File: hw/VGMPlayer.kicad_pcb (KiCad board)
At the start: 4 copper layers, 40 x 67 mm, 91 parts, among them J1 Micro_SD_Card, J2 EarPiece, P1 USB_C_Receptacle_16P, P2 SWD, P3 BATT, P4 UART, P5 ICSP, P6 CODEC, Q1 2N7002, Q2 AO3401A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

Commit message: 2nd version, change KBC functions
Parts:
- removed P4: UART, BZ_Connector:PINHDR-THT-50mil-01x02
- removed the R20 at (149.6, 100.6)
- added M1: Mechanical-NC, BZ_Mechanical:Hole-Mech_0.5, B.Cu at (131.5, 100.4)
- added R25: 1K, BZ_Resistor:R_0402, B.Cu at (131.8, 90.0)
- added R26: 1K, BZ_Resistor:R_0402, B.Cu at (131.8, 91.5)
- added S5: RESET, BZ_Switch:C&K_PTS525, F.Cu at (150.0, 127.5)
- C24, C34: value 10n -> DNP
- C25, C35: value 4.7u -> 10u
- C3, C4: value 33p -> 22p
- P2: footprint BZ_Connector:PINHDR-THT-50mil-01x05 -> BZ_Connector:PINHDR-THT-50mil-02x05
- R10, R9: value 2K -> 2K2
- R20: renamed from R21; value 2K -> 2K2
- TP1: footprint BZ_Misc:TE_RCT0805 -> BZ_Misc:TP_THT-Pad-0.8
- TP2: value BAT+ -> TP; footprint BZ_Misc:TE_RCT0805 -> BZ_Misc:TP_THT-Pad-0.8
- TP3: value BAT- -> TP; footprint BZ_Misc:TE_RCT0805 -> BZ_Misc:TP_THT-Pad-0.8
- U3, U7: value TPS79933DDCR -> LP5907MFX-3.3
- U5: value TP4057 -> MCP73831-OT; footprint BZ_Standard_IC:SOT-23-6 -> BZ_Standard_IC:SOT-23-5
- moved TP3 3.72 mm to (168.7, 96.7), turned to 270 degrees
- moved S3 3.00 mm to (142.0, 127.5), turned to 90 degrees
- moved S4 3.00 mm to (158.0, 127.5), turned to 270 degrees
- moved S2 2.30 mm to (150.0, 133.2)
- moved S1 2.30 mm to (150.0, 121.8)
- moved Y1 1.10 mm to (142.3, 104.3)
- moved C11 1.10 mm to (138.9, 103.3)
- moved C12 1.10 mm to (145.2, 98.7)
- moved C13 1.10 mm to (145.2, 94.9)
- moved C3 1.10 mm to (144.5, 103.3)
- moved C4 1.10 mm to (144.5, 105.3)
- moved C6 1.10 mm to (137.7, 103.3)
- moved R10 1.10 mm to (137.7, 105.3)
- moved R6 1.10 mm to (136.5, 103.3)
- moved R7 1.10 mm to (140.1, 103.3)
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- renumbered R22 to R21, R23 to R22, R24 to R23, R25 to R24
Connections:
- P2 pad 2: /SWCLK -> /SWDIO
- P2 pad 4: /SWDIO -> /SWCLK
- P2 pad 5: /RUN -> Net-(P2-Pad5)
- Q2 pad 2: VIN -> VBAT
- Q2 pad 3: VBAT -> VIN
- R20 pad 2: Net-(R21-Pad2) -> Net-(R20-Pad2)
- R21 pad 1: Net-(R21-Pad2) -> Net-(R20-Pad2)
- S4 pad 2: Net-(R20-Pad2) -> Net-(S4-Pad2)
- U5 pad 1: /CHG_CHRG -> (no net)
- U5 pad 5: (no net) -> Net-(R20-Pad2)
- U6 pad 2: /CHG_CHRG -> Net-(S4-Pad2)
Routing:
- net Net-(S4-Pad2): track 0.00 -> 37.7 mm, vias 0 -> 1
- net Net-(R20-Pad2): track 39.1 -> 3.88 mm, vias 1 -> 0
- net /VPP: track 30.0 -> 57.3 mm, vias 1 -> 3
- net /CHG_CHRG: track 18.3 -> 0.00 mm, vias 2 -> 0
- net VBAT: track 107.6 -> 95.2 mm, vias 3 -> 4
- net GND: track 182.5 -> 194.4 mm, vias 61 -> 58
- net Net-(P2-Pad8): track 0.00 -> 9.09 mm
- net 3V3: track 134.1 -> 141.5 mm
- net Net-(P2-Pad5): track 0.00 -> 7.23 mm, vias 0 -> 1
- net Net-(D2-PadK): track 51.2 -> 47.0 mm
- net /ICSPDAT: track 51.5 -> 47.4 mm
- net Net-(R21-Pad2): track 3.88 -> 0.00 mm
- net /SWDIO: track 7.32 -> 10.5 mm
- net Net-(S2-Pad2): track 37.7 -> 35.6 mm
- net /SD_DAT0: track 21.0 -> 19.0 mm
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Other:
- board text added: "C"
- board text added: "D"
- board text added: "E"
- board text added: "G"
- board text added: "V"
- board text added: "VGMPlayer 20210604"
- board text removed: "+USB"
- board text removed: "3V"
- board text removed: "3V3"
- board text removed: "BOOTSEL"
- board text removed: "CLK"
- board text removed: "DFU"
- board text removed: "DIO"
- board text removed: "Dev. Mode"
- board text removed: "EN"
- board text removed: "GD"
- board text removed: "GND"
- board text removed: "IO"
- board text removed: "RUN"
- board text removed: "TEST"
- board text removed: "VGMPlayer 20210517"

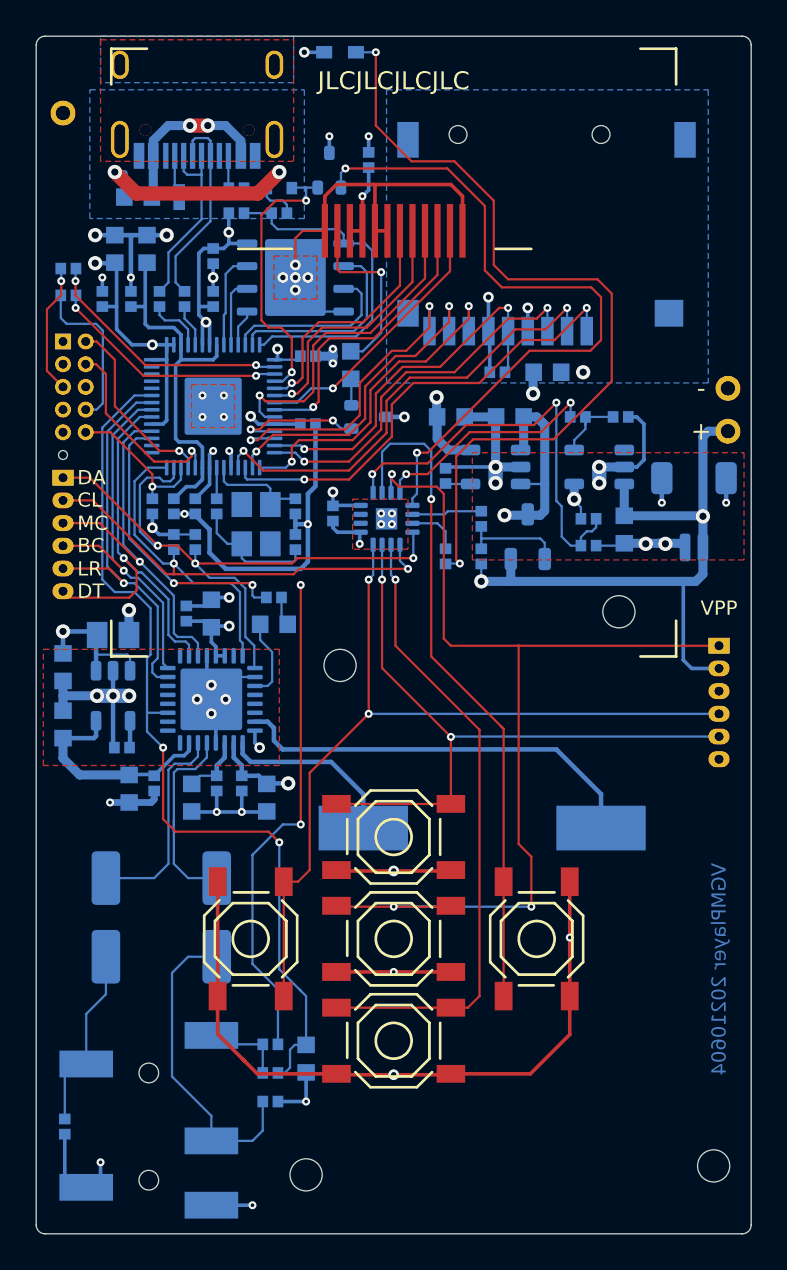
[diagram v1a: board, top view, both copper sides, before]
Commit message: Using Molex Picoblade 1.25 connector
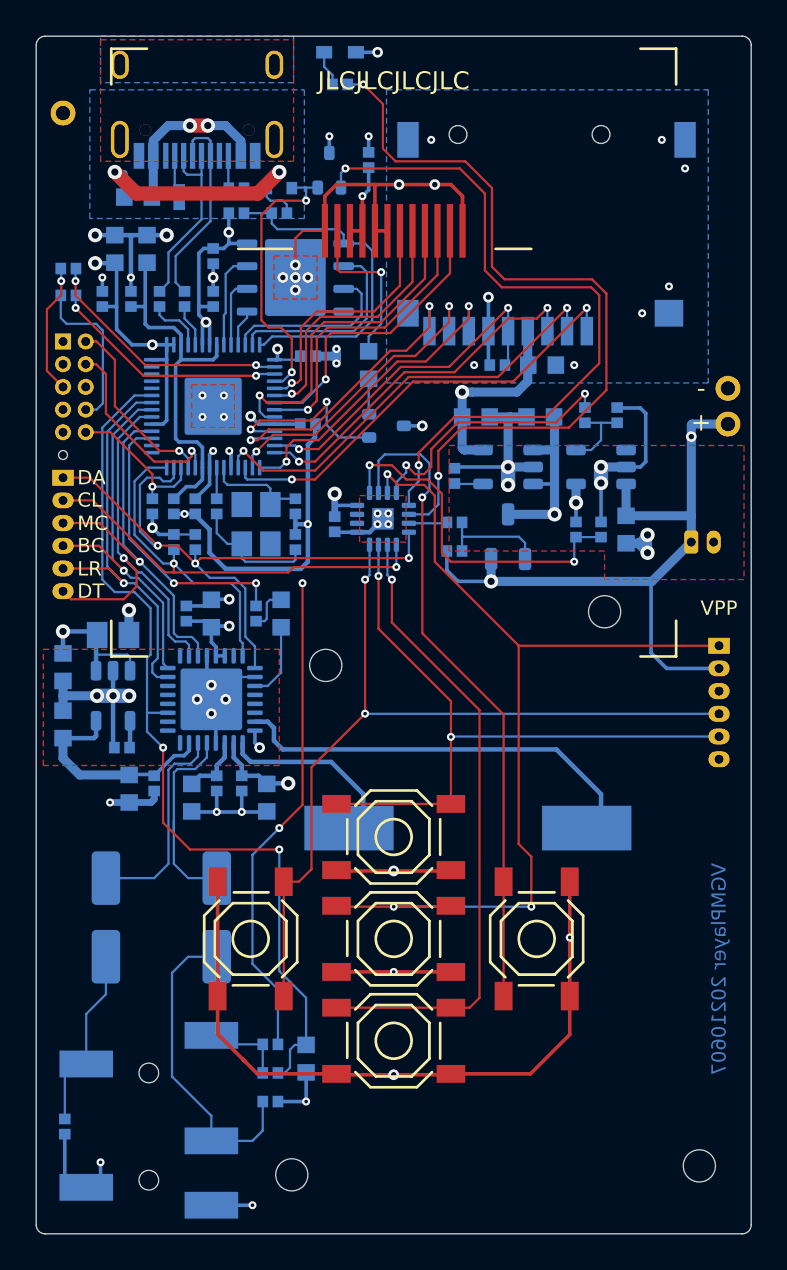
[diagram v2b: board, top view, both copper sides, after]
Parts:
- P3: footprint BZ_Connector:JST_SM02B-SRSS-TB -> BZ_Connector:MLX_PicoBlade-Horz-01x02-1.25P
- moved R24 27.1 mm to (147.0, 79.7), turned to 0 degrees
- moved P3 1.71 mm to (166.7, 105.3)
- moved C33 1.70 mm to (158.2, 98.3)
- moved R22 1.53 mm to (153.4, 105.8), turned to 0 degrees
- moved R23 1.51 mm to (153.4, 104.2), turned to 180 degrees
- moved C35 1.40 mm to (154.6, 98.3)
- moved R13 1.35 mm to (142.3, 109.3), turned to 90 degrees
- moved R19 1.14 mm to (161.6, 104.6), turned to 270 degrees
- moved Q1 1.12 mm to (149.6, 98.8)
- moved Q2 1.10 mm to (156.4, 105.0)
- moved R12 1.00 mm to (148.6, 95.4)
- moved R18 0.92 mm to (160.2, 104.6), turned to 90 degrees
- moved SP1 0.80 mm to (153.8, 144.0)
- moved C14 0.72 mm to (143.7, 109.3), turned to 90 degrees
- moved U7 0.70 mm to (156.4, 101.1)
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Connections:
- P3 pad 1: GND -> VBAT
- P3 pad 2: VBAT -> GND
- U6 pad 6: Net-(R23-Pad2) -> Net-(R24-Pad2)
- U6 pad 7: Net-(R24-Pad2) -> Net-(R23-Pad2)
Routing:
- net Net-(D2-PadK): track 47.0 -> 1.99 mm, vias 2 -> 0
- net Net-(R24-Pad2): track 3.01 -> 44.4 mm, vias 0 -> 2
- net VBAT: track 95.2 -> 89.5 mm
- net /USB_DET: track 24.0 -> 19.9 mm
- net /LCD_BL: track 7.40 -> 10.4 mm
- net /VPP: track 57.3 -> 54.8 mm
- net /CHG_CTL: track 13.1 -> 15.2 mm
- net Net-(R23-Pad2): track 3.92 -> 2.10 mm
- net 3V3: track 141.5 -> 139.7 mm, vias 15 -> 13
- net GND: track 194.4 -> 192.9 mm, vias 58 -> 63
- net /SD_CLK: track 21.1 -> 19.7 mm
- net /LCD_RES: track 15.1 -> 16.5 mm
- net VIN: track 41.2 -> 42.4 mm
- net Net-(Q3-Pad1): track 38.9 -> 40.0 mm
- net /SD_DAT2: track 26.2 -> 25.2 mm
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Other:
- board text added: "VGMPlayer 20210607"
- board text removed: "VGMPlayer 20210604"

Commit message: Fix wrong 2N7002 pinout
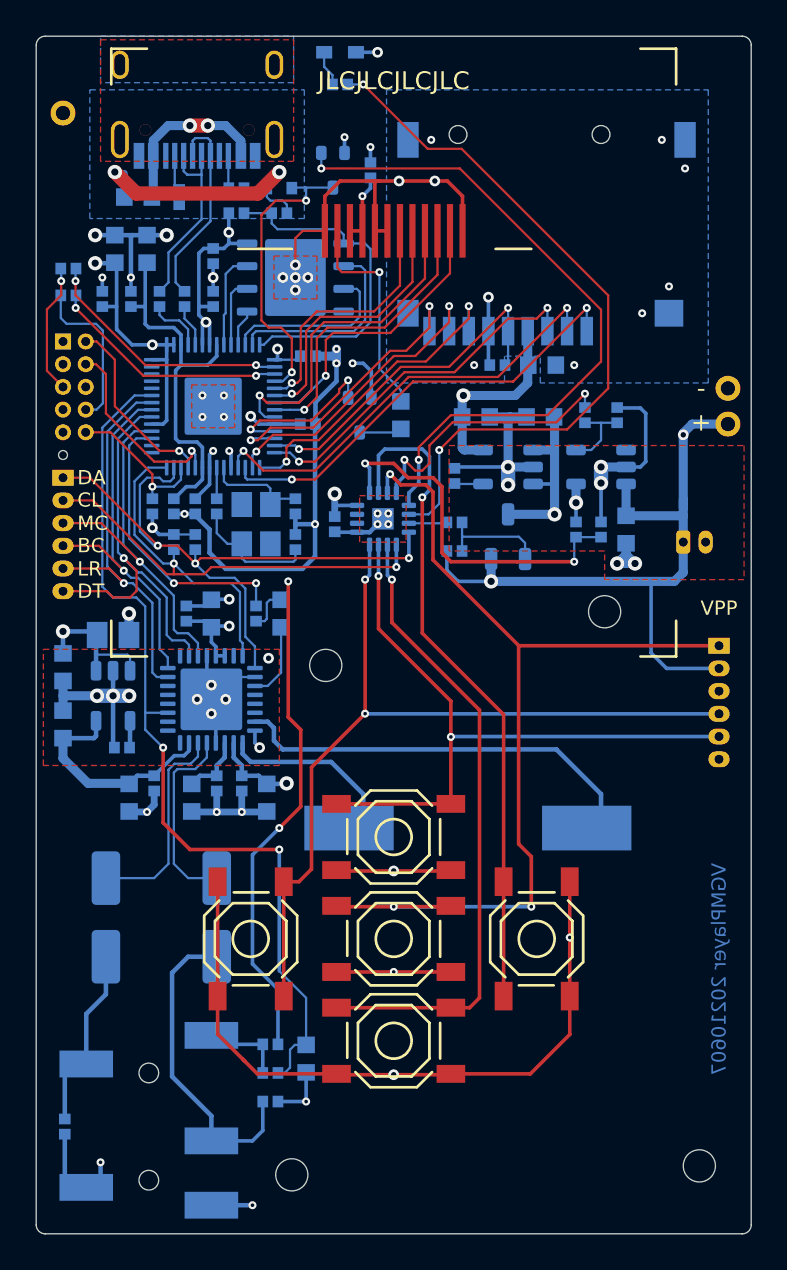
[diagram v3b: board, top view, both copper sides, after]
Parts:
- moved R12 3.33 mm to (150.4, 98.2)
- moved Q1 1.62 mm to (148.1, 98.2), turned to 90 degrees
- moved C16 0.58 mm to (148.7, 84.5)
- moved C20 0.50 mm to (135.2, 119.6)
- moved P3 0.45 mm to (166.2, 105.3)
- moved Q3 0.20 mm to (146.6, 84.5), turned to 90 degrees
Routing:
- net GND: track 192.9 -> 199.1 mm, vias 63 -> 64
- net Net-(R24-Pad2): track 44.4 -> 40.4 mm
- net Net-(DISP1-Pad2): track 9.39 -> 12.2 mm
- net 3V3: track 139.7 -> 137.7 mm
- net Net-(Q3-Pad1): track 40.0 -> 38.4 mm
- net Net-(C21-Pad1): track 32.2 -> 30.9 mm
- net /LCD_BL: track 10.4 -> 9.27 mm
- net Net-(Q1-Pad3): track 1.99 -> 2.95 mm
- net /BOOT: track 16.1 -> 17.0 mm
- net /USB_DET: track 19.9 -> 20.7 mm
- net Net-(S4-Pad2): track 36.9 -> 37.5 mm
- net Net-(C28-Pad1): track 11.4 -> 10.8 mm

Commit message: Checkin before fab 20210610
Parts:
- removed the R22 at (153.4, 105.8)
- added C36: 100n, BZ_Capacitor:C_0402, B.Cu at (151.8, 99.5)
- added D2: B0540WS, BZ_Diode:D_SOD-323, B.Cu at (159.0, 104.9)
- added Q1: AO3401A, BZ_Standard_IC:SOT-23-3, B.Cu at (162.2, 103.6)
- added R24: 1M5, BZ_Resistor:R_0402, B.Cu at (153.1, 99.5)
- added REF**: JLC_Position, BZ_Mechanical:JLC_Position, F.Cu at (168.5, 142.5)
- added REF**: JLC_Position, BZ_Mechanical:JLC_Position, F.Cu at (168.5, 78.5)
- added REF**: JLC_Position, BZ_Mechanical:JLC_Position, F.Cu at (131.5, 78.5)
- added S4: D, BZ_Switch:C&K_PTS525, F.Cu at (150.0, 133.2)
- R18: value 10K -> 5K1
- R20: value 2K2 -> 100K
- R23: value 10K -> 100K
- S5: renamed from S2; value D -> ENTER
- S6: renamed from S5; footprint BZ_Switch:C&K_PTS525 -> BZ_Switch:SW-PUSH_3x2x0.6H; moved to B.Cu
- moved S6 24.2 mm to (168.2, 111.6), turned to 270 degrees
- moved R21 10.9 mm to (153.1, 103.7)
- moved R20 10.7 mm to (153.1, 105.8), turned to 90 degrees
- moved R18 7.60 mm to (162.3, 97.3), turned to 0 degrees
- moved C31 6.16 mm to (168.2, 107.9), turned to 0 degrees
- moved S5 5.70 mm to (150.0, 127.5)
- moved C34 4.48 mm to (155.6, 97.7), turned to 0 degrees
- moved C35 4.40 mm to (159.0, 98.1), turned to 270 degrees
- moved P5 4.26 mm to (168.2, 115.4)
- moved C33 3.10 mm to (159.0, 101.3), turned to 90 degrees
- moved C16 2.80 mm to (147.1, 86.8), turned to 180 degrees
- moved R23 2.62 mm to (153.1, 101.6), turned to 90 degrees
- moved R19 2.11 mm to (162.7, 106.4), turned to 180 degrees
- moved U5 1.57 mm to (162.3, 99.7)
- moved Q3 0.81 mm to (147.0, 83.8)
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- renumbered D2 to D3, Q1 to Q4, R24 to R22, S3 to S1, S4 to S2, S1 to S3
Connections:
- C31 pad 1: VBAT -> /BATT
- C32 pad 2: VBAT -> VRAW
- D3 pad A: VBAT -> Net-(D3-PadA)
- D3 pad K: Net-(D2-PadK) -> GND
- P3 pad 1: VBAT -> /BATT
- P5 pad 2: VBAT -> VRAW
- Q2 pad 2: VBAT -> VRAW
- R18 pad 1: /USB_DET -> Net-(R18-Pad1)
- R18 pad 2: VUSB -> GND
- R19 pad 1: GND -> VUSB
- R19 pad 2: /USB_DET -> GND
- R20 pad 1: /CHG_CTL -> VRAW
- R20 pad 2: Net-(R20-Pad2) -> Net-(Q2-Pad1)
- R21 pad 1: Net-(R20-Pad2) -> Net-(Q2-Pad1)
- R21 pad 2: GND -> Net-(R21-Pad2)
- R22 pad 1: Net-(D2-PadK) -> Net-(R22-Pad1)
- R22 pad 2: Net-(R24-Pad2) -> Net-(D3-PadA)
- R23 pad 1: Net-(Q2-Pad1) -> /BATT
- R23 pad 2: Net-(R23-Pad2) -> Net-(C36-Pad1)
- TP2 pad 1: VBAT -> /BATT
- U5 pad 3: VBAT -> /BATT
- U5 pad 5: Net-(R20-Pad2) -> Net-(R18-Pad1)
- U6 pad 1: /USB_DET -> Net-(S4-Pad2)
- U6 pad 16: VBAT -> VRAW
- U6 pad 4: /CHG_CTL -> Net-(Q3-Pad1)
- U6 pad 5: Net-(Q3-Pad1) -> Net-(R22-Pad1)
- U6 pad 6: Net-(R24-Pad2) -> Net-(C36-Pad1)
- U6 pad 7: Net-(R23-Pad2) -> Net-(R21-Pad2)
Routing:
- net VBAT: track 89.9 -> 0.00 mm, vias 4 -> 0
- net Net-(S4-Pad2): track 0.00 -> 44.0 mm, vias 0 -> 1
- net VRAW: track 0.00 -> 43.8 mm, vias 0 -> 2
- net Net-(R22-Pad1): track 0.00 -> 41.5 mm, vias 0 -> 2
- net Net-(R24-Pad2): track 40.4 -> 0.00 mm, vias 2 -> 0
- net /BATT: track 0.00 -> 33.2 mm, vias 0 -> 2
- net /USB_DET: track 20.7 -> 0.00 mm, vias 2 -> 0
- net /VPP: track 54.8 -> 35.4 mm, vias 3 -> 1
- net /CHG_CTL: track 15.5 -> 0.00 mm, vias 2 -> 0
- net GND: track 199.1 -> 209.2 mm, vias 64 -> 84
- net VUSB: track 54.4 -> 63.1 mm
- net Net-(C36-Pad1): track 0.00 -> 6.47 mm
- net Net-(S5-Pad2): track 35.6 -> 30.4 mm
- net VIN: track 42.0 -> 36.9 mm
- net Net-(R20-Pad2): track 4.40 -> 0.00 mm
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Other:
- board text added: "VGMPlayer 20210610"
- board text removed: "VGMPlayer 20210607"

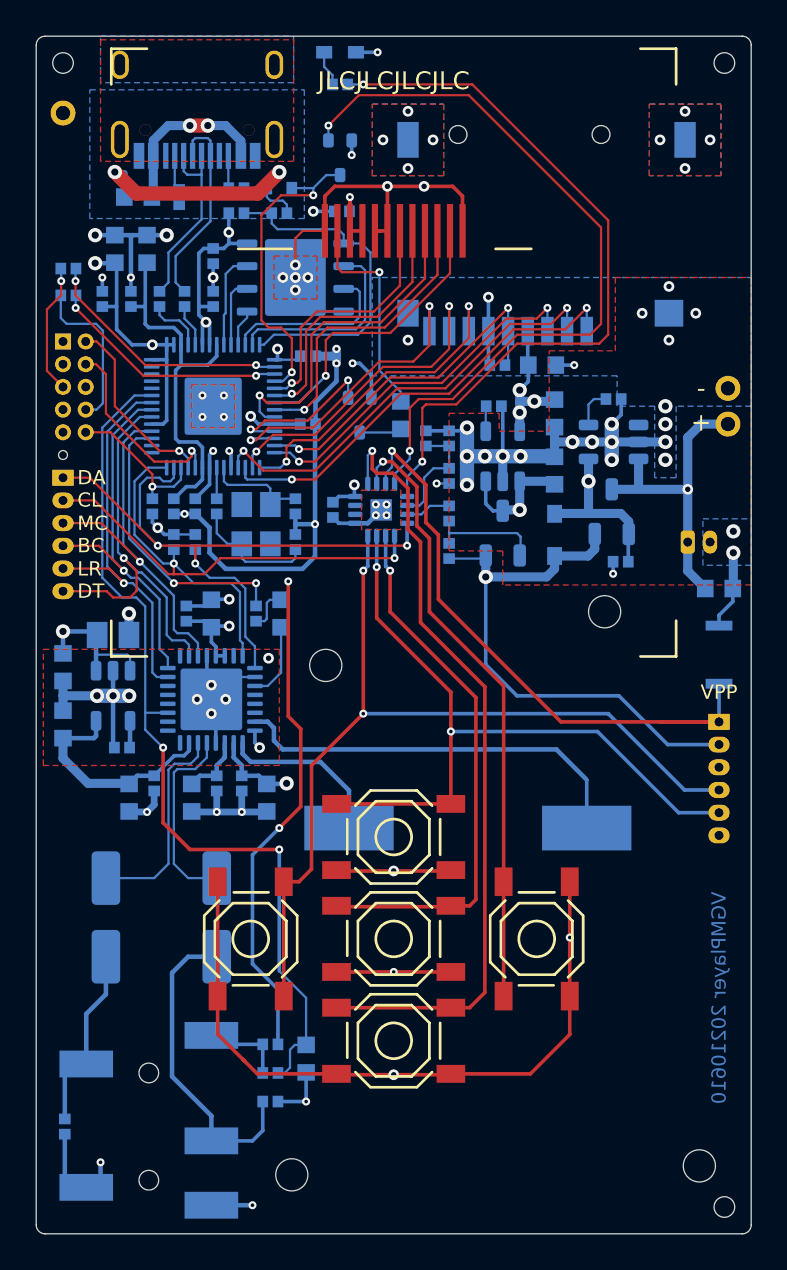
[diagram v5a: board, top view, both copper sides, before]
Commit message: Change to 4 buttons, layout adjust to casing design
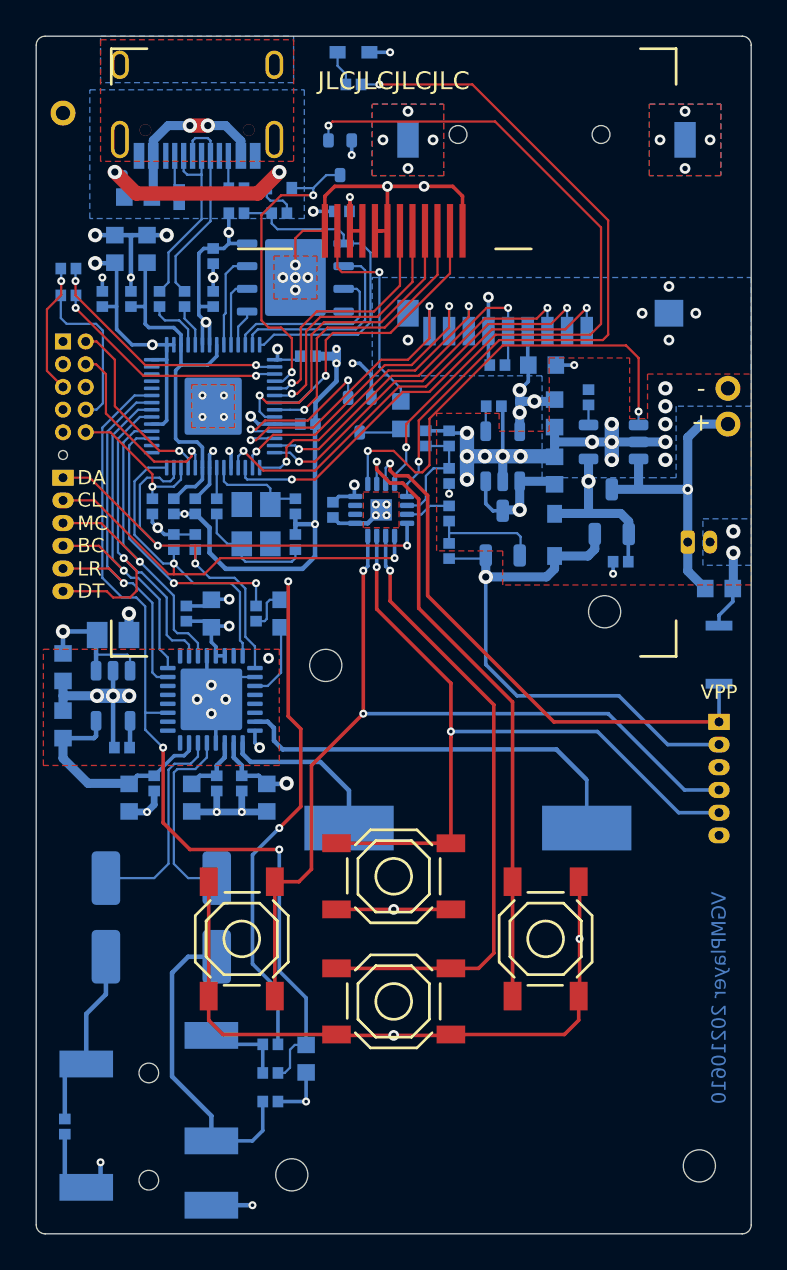
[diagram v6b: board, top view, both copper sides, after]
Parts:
- removed REF** (x3): JLC_Position, BZ_Mechanical:JLC_Position
- removed the S5 at (150.0, 127.5)
- R10, R9: value 2K2 -> 2.2K
- R18: value 5K1 -> 5.1K
- moved S3 2.20 mm to (150.0, 124.0)
- moved S4 2.20 mm to (150.0, 131.0)
- moved R18 1.40 mm to (160.9, 97.2), turned to 90 degrees
- moved D3 0.75 mm to (147.8, 77.9)
- moved R22 0.75 mm to (147.8, 79.7)
- moved S1 0.50 mm to (141.5, 127.5)
- moved S2 0.50 mm to (158.5, 127.5)
- renumbered S6 to S5
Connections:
- U5 pad 1: (no net) -> Net-(U5-Pad1)
- U6 pad 1: Net-(S4-Pad2) -> Net-(U5-Pad1)
- U6 pad 10: Net-(S5-Pad2) -> Net-(S4-Pad2)
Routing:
- net Net-(S5-Pad2): track 30.4 -> 0.00 mm, vias 1 -> 0
- net Net-(U5-Pad1): track 0.00 -> 26.0 mm, vias 0 -> 2
- net GND: track 209.2 -> 198.6 mm, vias 84 -> 83
- net Net-(S4-Pad2): track 44.0 -> 35.0 mm
- net /VPP: track 35.4 -> 31.3 mm
- net /ICSPCLK: track 40.0 -> 42.2 mm
- net /BATT: track 33.2 -> 31.5 mm
- net Net-(Q3-Pad1): track 42.5 -> 40.9 mm
- net VUSB: track 63.1 -> 61.6 mm
- net Net-(R18-Pad1): track 2.25 -> 1.15 mm
- net Net-(R22-Pad1): track 41.5 -> 40.5 mm
- net /SD_DAT0: track 18.6 -> 17.9 mm
- net /SD_DAT1: track 18.2 -> 17.5 mm
- net /ICSPDAT: track 49.9 -> 50.4 mm
